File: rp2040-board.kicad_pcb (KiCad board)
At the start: 4 copper layers, 105.3 x 75.1 mm, 159 parts, among them J1 24V IN, J10 E0-RUNOUT, J11 FAN1, J12 FAN2, J13 FAN3, J14 HB, J15 E0, J16 TH-E0, J17 X-STEPPER, J18 Y-STEPPER, J19 ZA-STEPPER, J2 USB4105-GF-A, J20 E0-STEPPER, J21 ZB-STEPPER, J22 Exp. Header 2, J23 Exp. Header 3, J3 PGA2040, J4 Exp. Header 1, J5 PROBE, J6 X-ENDSTOP, J7 TH-HB, J8 Y-ENDSTOP, J9 Z-ENDSTOP, Q1 AO3400C, Q2 AO3400C, Q3 AO3400C, U1 AMS1117-3.3, U2 TPS5450DDAR, U3 74HCT365D,653, U4 FDS8896, U5 FDS8896, U6 TMC2226-SA-T, U7 TMC2226-SA-T, U8 TMC2226-SA-T, U9 TMC2226-SA-T

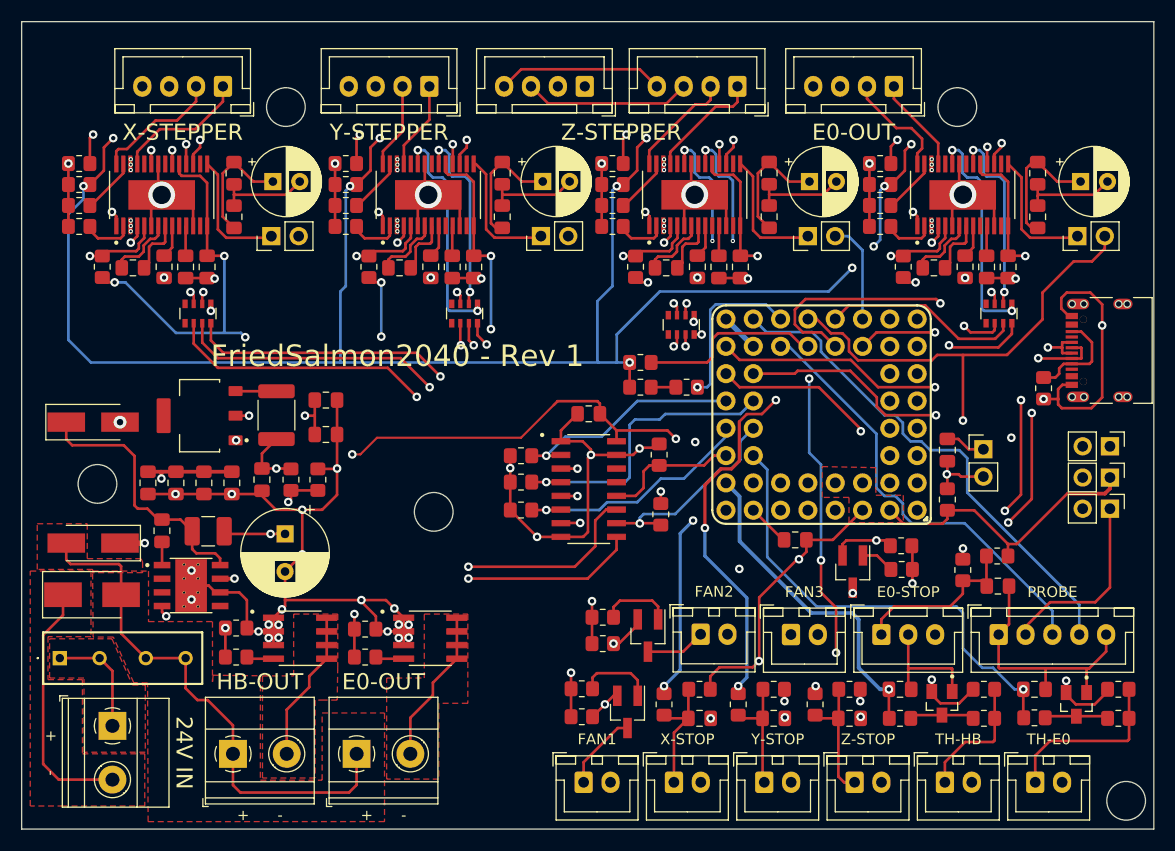
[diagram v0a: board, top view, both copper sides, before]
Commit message: Rev 1.1 - PT1000 + ADC/I2C GPIO
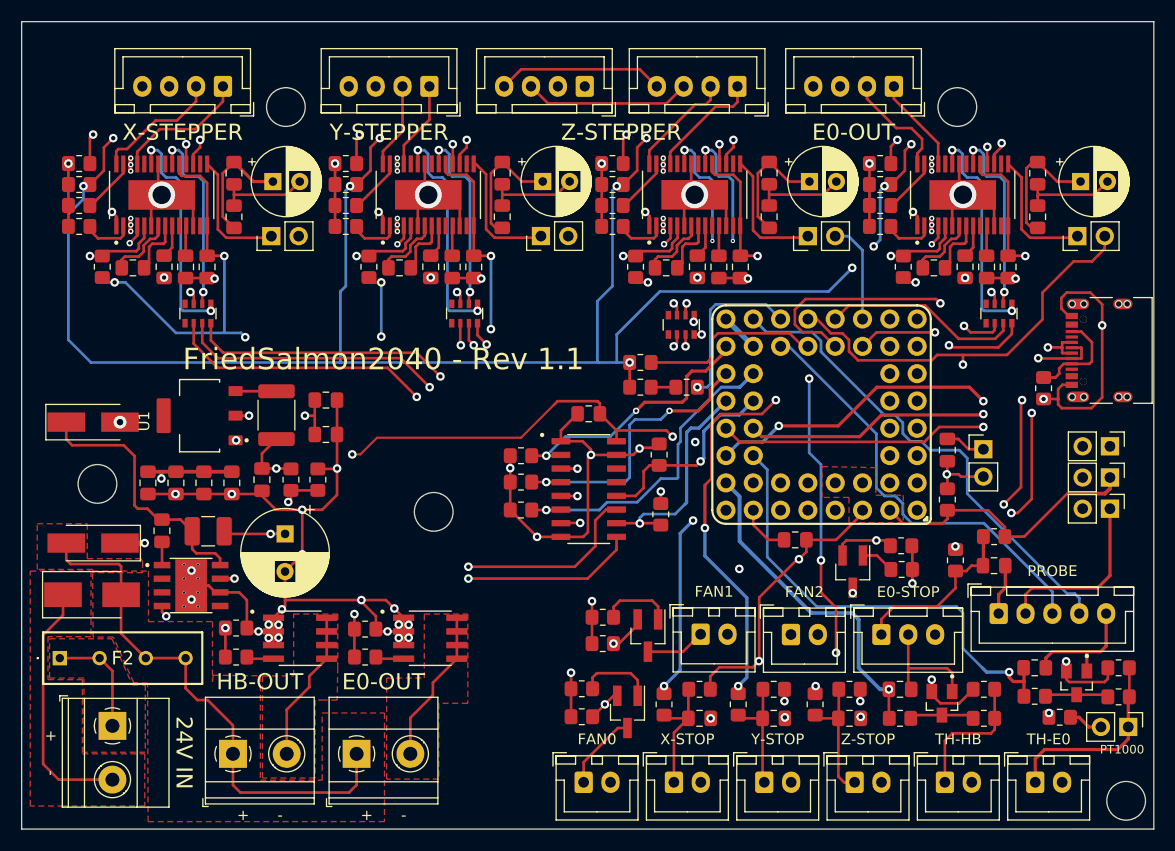
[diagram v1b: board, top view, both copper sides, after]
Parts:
- added JP6: PT1000, Connector_PinHeader_2.54mm:PinHeader_1x02_P2.54mm_Vertical, F.Cu at (200.6, 128.6)
- added R57: 2.37K, Resistor_SMD:R_0805_2012Metric_Pad1.20x1.40mm_HandSolder, F.Cu at (194.2, 127.7)
- J11: value FAN1 -> FAN0
- J12: value FAN2 -> FAN1
- J13: value FAN3 -> FAN2
- moved C18 2.00 mm to (191.9, 123.1)
- moved D5 2.00 mm to (195.8, 124.5)
- moved R25 2.00 mm to (191.9, 125.8)
- moved R32 2.00 mm to (199.7, 125.8)
- moved R33 2.00 mm to (199.7, 123.1)
- moved J5 1.95 mm to (188.5, 118.1)
- moved C17 1.93 mm to (188.1, 113.6)
- moved R20 1.82 mm to (188.1, 110.9)
- moved R14 1.13 mm to (184.5, 113.1)
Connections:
- J22 pad 2: GPIO22 -> GPIO25
- J3 pad C8: /HB_PWM -> GPIO27
- J3 pad D7: /E0_PWM -> GPIO26
- J3 pad D8: /FAN3_PWM -> GPIO25
- J3 pad E7: /FAN2_PWM -> /HB_PWM
- J3 pad E8: /FAN1_PWM -> /E0_PWM
- J3 pad F7: GPIO22 -> /FAN2_PWM
- J3 pad F8: GPIO21 -> /FAN1_PWM
- J3 pad G8: GPIO20 -> /FAN0_PWM
- J4 pad 1: GPIO20 -> GPIO27
- J4 pad 2: GPIO21 -> GPIO26
- R7 pad 2: /FAN3_PWM -> /FAN2_PWM
- R8 pad 2: /FAN2_PWM -> /FAN1_PWM
- R9 pad 2: /FAN1_PWM -> /FAN0_PWM
- U3 pad 2: /FAN1_PWM -> /FAN0_PWM
- U3 pad 4: /FAN2_PWM -> /FAN1_PWM
- U3 pad 6: /FAN3_PWM -> /FAN2_PWM
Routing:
- net GPIO27: track 0.00 -> 41.5 mm, vias 0 -> 2
- net GPIO20: track 40.2 -> 0.00 mm, vias 1 -> 0
- net GPIO21: track 39.6 -> 0.00 mm, vias 1 -> 0
- net GPIO22: track 37.4 -> 0.00 mm, vias 2 -> 0
- net GPIO25: track 0.00 -> 36.2 mm, vias 0 -> 1
- net GPIO26: track 0.00 -> 33.1 mm, vias 0 -> 1
- net /FAN0_PWM: track 0.00 -> 25.0 mm, vias 0 -> 2
- net /FAN3_PWM: track 23.0 -> 0.00 mm, vias 1 -> 0
- net GND: track 245.7 -> 237.5 mm
- net /HB_PWM: track 12.6 -> 18.7 mm, vias 0 -> 1
- net /FAN1_PWM: track 21.5 -> 27.0 mm, vias 1 -> 2
- net +3.3V: track 355.8 -> 359.6 mm, vias 19 -> 20
- net Net-(JP6-Pad2): track 0.00 -> 3.21 mm
- net +5V: track 127.0 -> 124.9 mm
- net /FAN2_PWM: track 28.0 -> 29.7 mm
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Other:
- board text added: "FAN0"
- board text added: "FriedSalmon2040 - Rev 1.1"
- board text added: "PT1000"
- board text removed: "FAN3"
- board text removed: "FriedSalmon2040 - Rev 1"

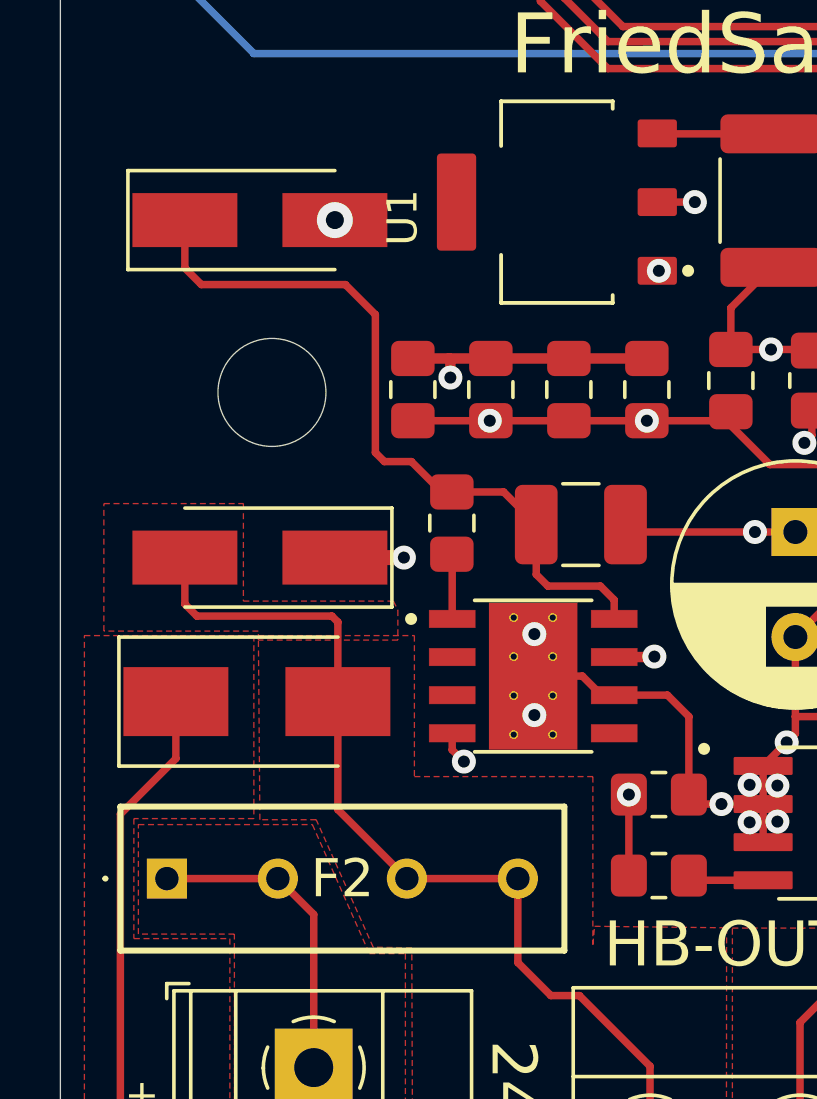
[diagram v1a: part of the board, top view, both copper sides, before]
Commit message: Change Inductor & PT1000 Resistor
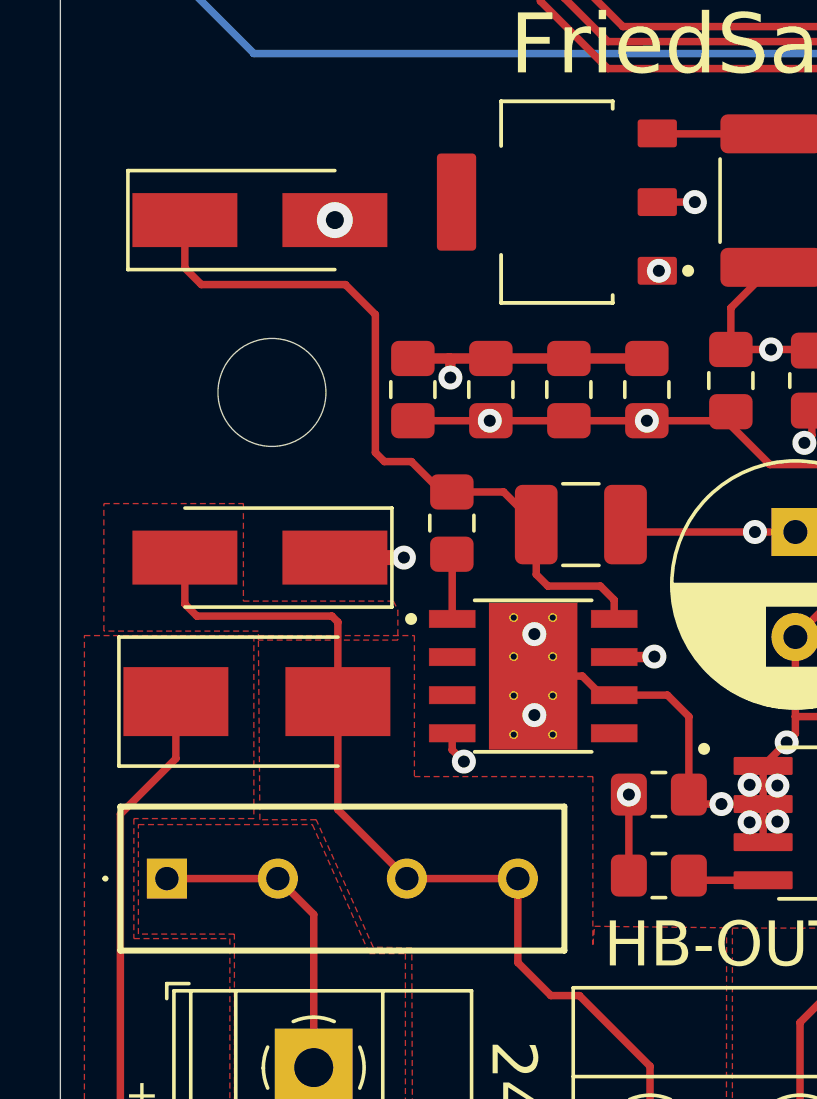
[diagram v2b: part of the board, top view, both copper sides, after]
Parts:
- R57: value 2.37K -> 4.7K
